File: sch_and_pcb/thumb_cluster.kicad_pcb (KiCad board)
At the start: 2 copper layers, 34 parts, among them J1 8PIN_CONN, J2 8PIN_CONN

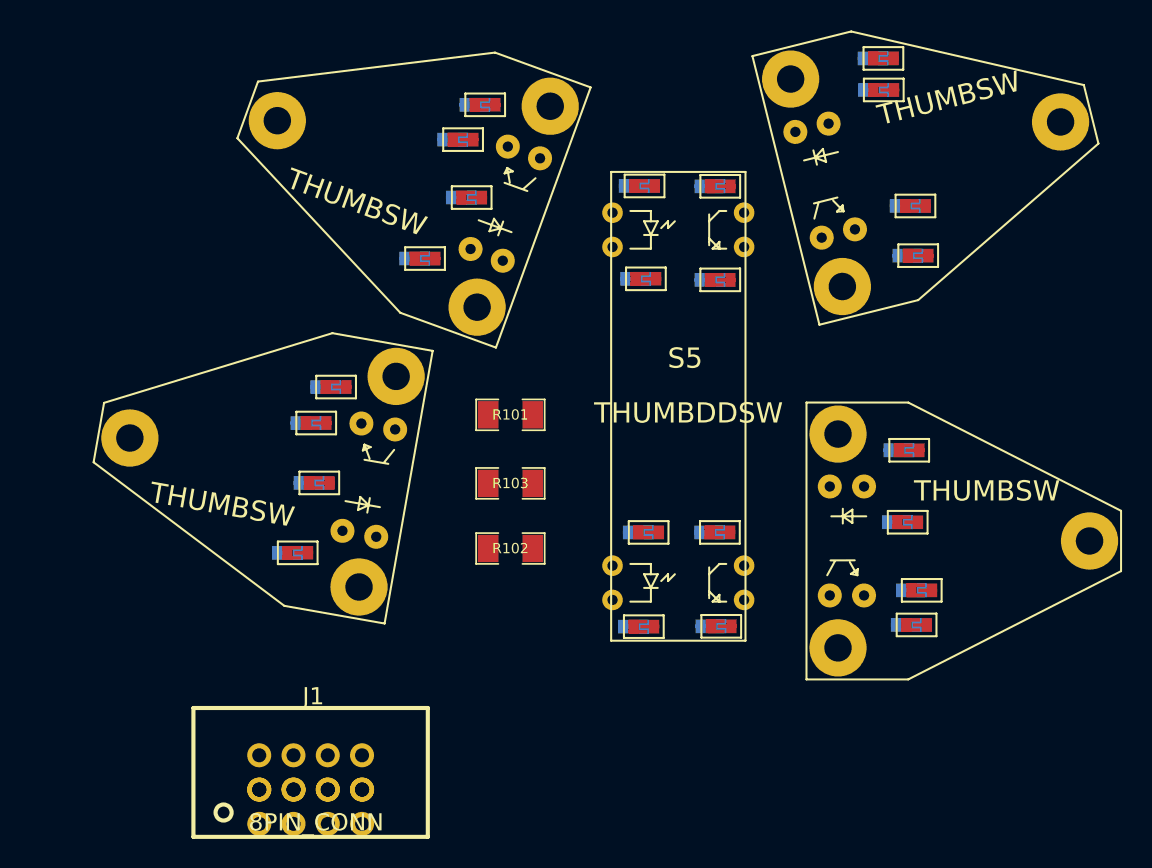
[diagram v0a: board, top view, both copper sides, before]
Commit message: PCB mostly routed. Shape not yet defined.
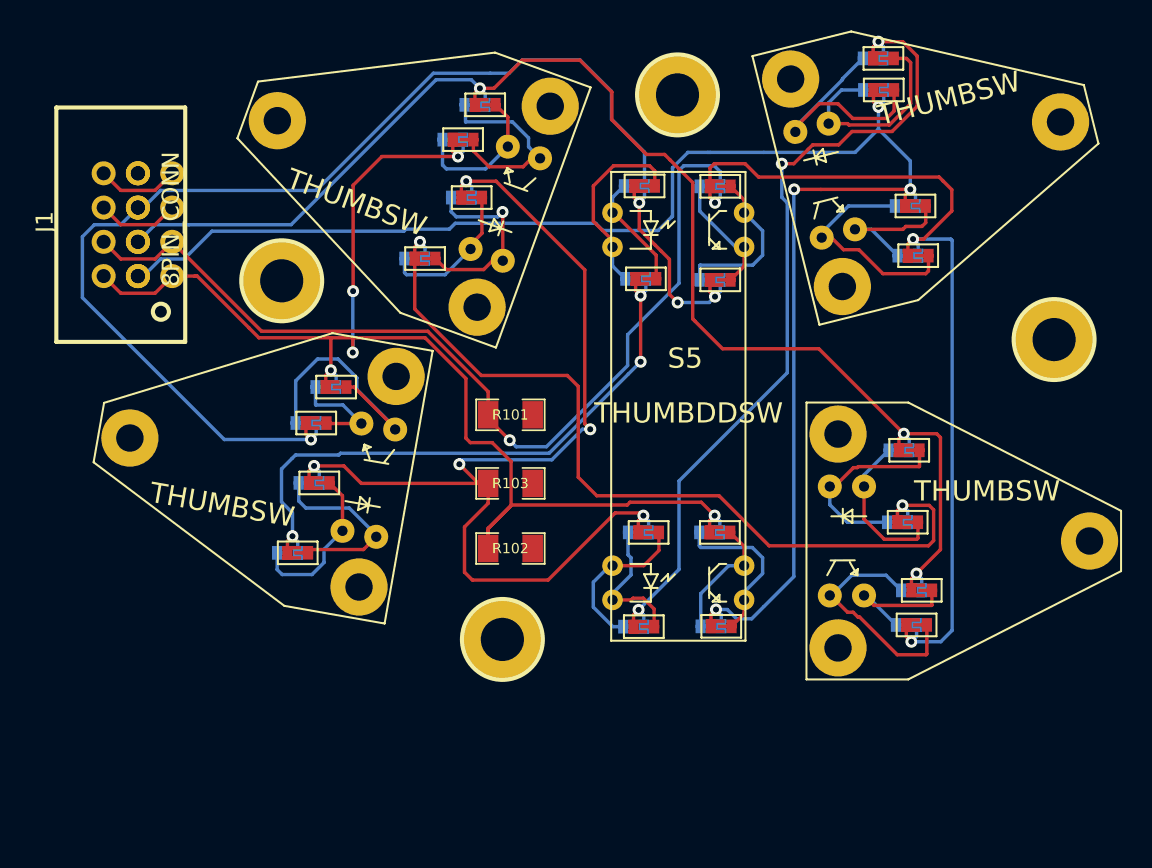
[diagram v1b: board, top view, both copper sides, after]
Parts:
- added M3_Mounting_Hole: VAL**, DodoHand:M3_Mounting_Hole, F.Cu at (-29.4, -9.30)
- added M3_Mounting_Hole: VAL**, DodoHand:M3_Mounting_Hole, F.Cu at (27.9, -4.95)
- added M3_Mounting_Hole: VAL**, DodoHand:M3_Mounting_Hole, F.Cu at (-13.0, 17.3)
- added M3_Mounting_Hole: VAL**, DodoHand:M3_Mounting_Hole, F.Cu at (-0.06, -23.1)
- moved J2 44.7 mm to (-38.8, -13.5), turned to 90 degrees
- moved J1 43.0 mm to (-41.3, -13.5), turned to 90 degrees
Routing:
- net /COL4: track 0.00 -> 139.4 mm, vias 0 -> 4
- net /ROW0: track 0.00 -> 122.1 mm, vias 0 -> 4
- net /ROW1: track 0.00 -> 103.5 mm, vias 0 -> 3
- net /ROW2: track 0.00 -> 99.3 mm, vias 0 -> 4
- net /COL5: track 0.00 -> 99.2 mm, vias 0 -> 5
- net Net-(R103-Pad1): track 0.00 -> 81.9 mm, vias 0 -> 5
- net Net-(SB5-Pad1): track 0.00 -> 63.9 mm, vias 0 -> 2
- net Net-(SB4-Pad1): track 0.00 -> 62.2 mm, vias 0 -> 3
- net Net-(SB6-Pad1): track 0.00 -> 45.7 mm, vias 0 -> 3
- net Net-(S4-Pad4): track 0.00 -> 19.5 mm
- net Net-(S1-Pad2): track 0.00 -> 18.8 mm
- net Net-(S3-Pad4): track 0.00 -> 18.2 mm
- net Net-(S1-Pad4): track 0.00 -> 17.5 mm
- net Net-(S1-Pad1): track 0.00 -> 16.7 mm
- net Net-(S2-Pad4): track 0.00 -> 15.5 mm
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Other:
- net class Default: clearance 0.254 -> 0.2286
- rule trace_clearance: 0.254 -> 0.2286
- rule trace_min: 0.254 -> 0.2286

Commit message: ground plane connected. silk cleanup still needed. soldermask slightly wrong on solder bridge. Needs corrected.
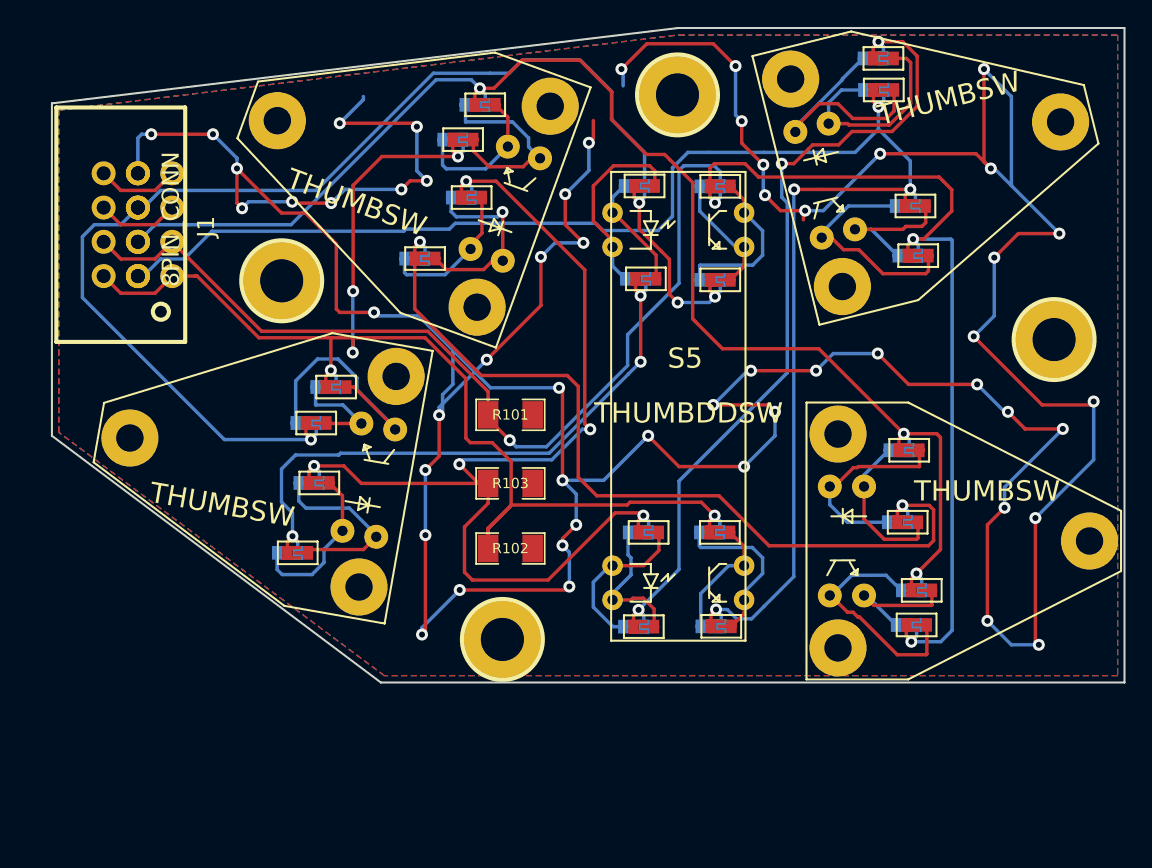
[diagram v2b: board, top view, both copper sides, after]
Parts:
- added G***: DHLOGO, DodoHand:DHLOGO, B.Cu at (-10.9, 2.13)
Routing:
- net GND: track 0.00 -> 340.6 mm, vias 0 -> 53
- added copper zone on B.Cu, net GND
- added copper zone on F.Cu, net GND
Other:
- board outline added: 79.5 x 48.5 mm
- net class Default: clearance 0.2286 -> 0.127
- rule trace_clearance: 0.2286 -> 0.127

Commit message: First pass of the Thumb Cluster PCB is complete.
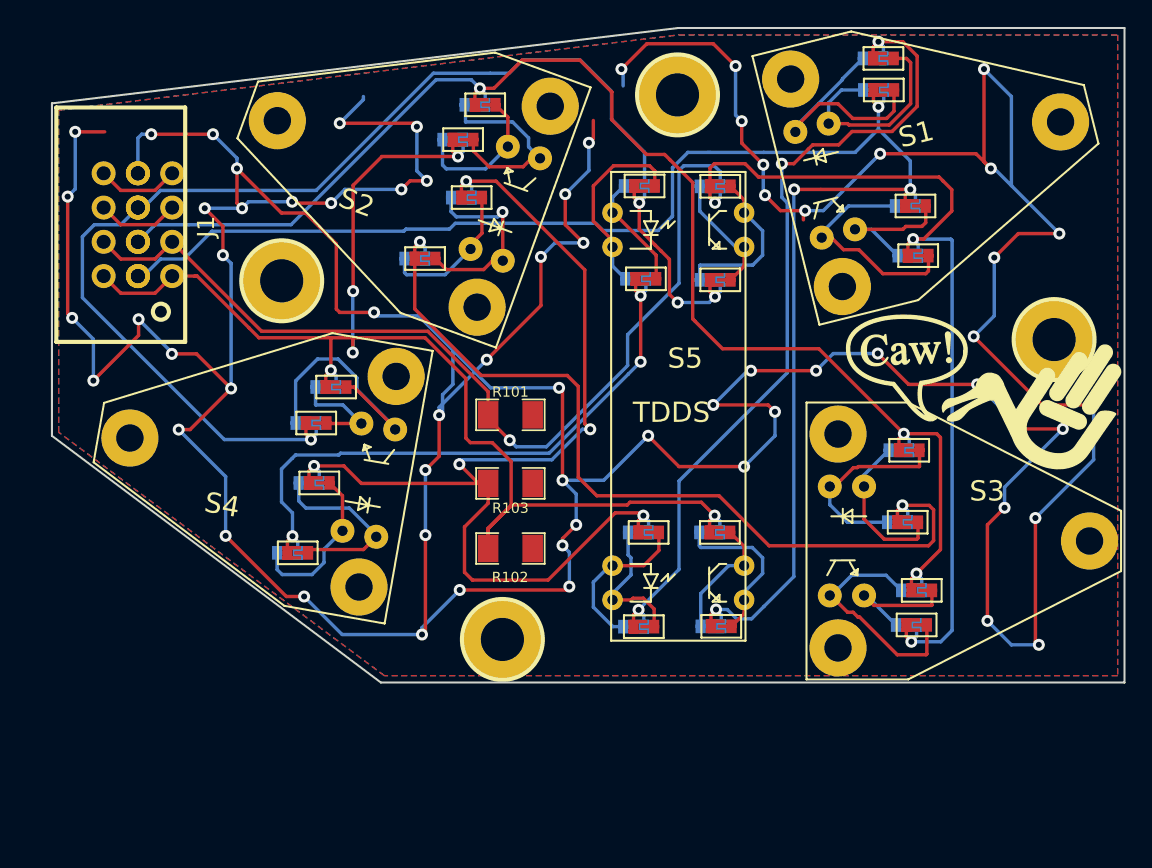
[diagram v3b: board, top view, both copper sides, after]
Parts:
- G***: moved to F.Cu
- S1: value THUMBSW -> S1
- S2: value THUMBSW -> S2
- S3: value THUMBSW -> S3
- S4: value THUMBSW -> S4
- S5: value THUMBDDSW -> TDDS
- moved G*** 33.7 mm to (22.6, -1.07), turned to 0 degrees
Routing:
- net GND: track 340.6 -> 426.2 mm, vias 53 -> 65
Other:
- board text added: "Solder bridges only on opposite side of opto parts."
- board text added: "Thanks to regack for the solder bridge science support"

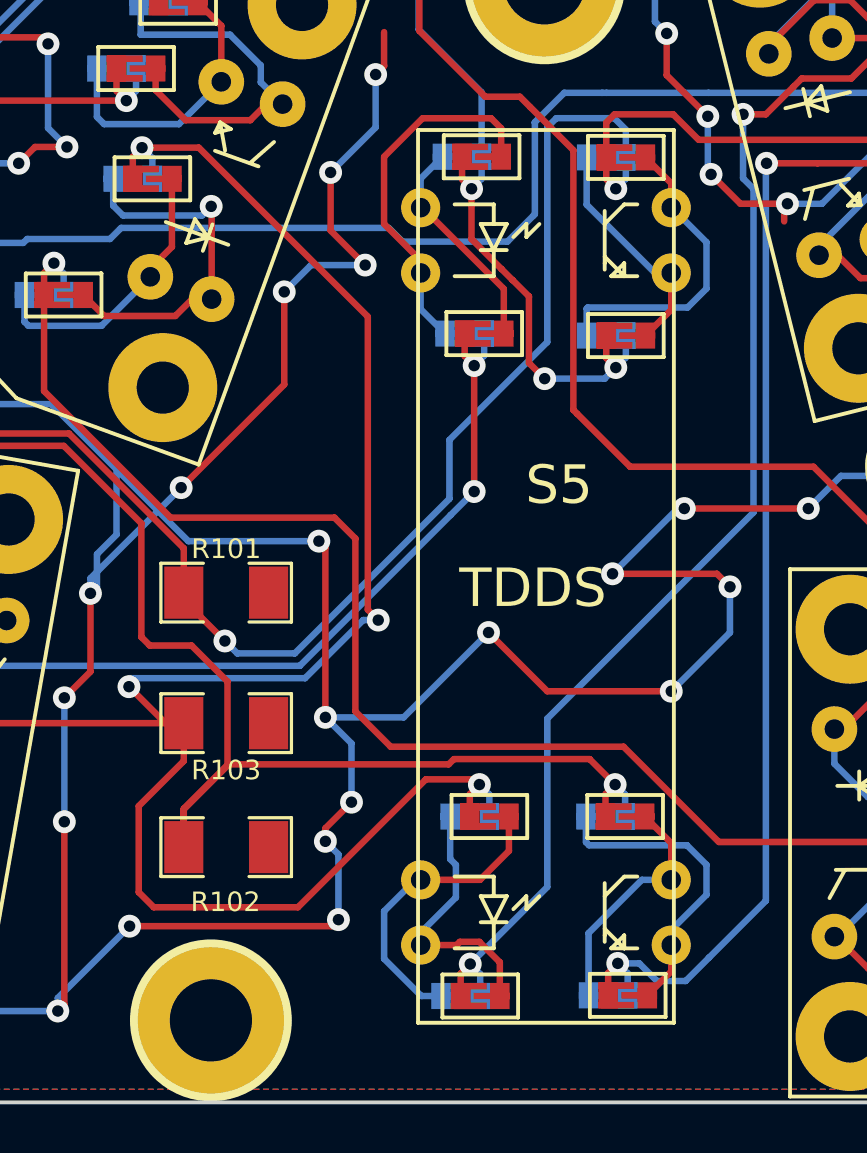
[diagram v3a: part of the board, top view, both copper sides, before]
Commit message: Corrected TDDS footprint, had to put it into new library in new .pretty directory format.
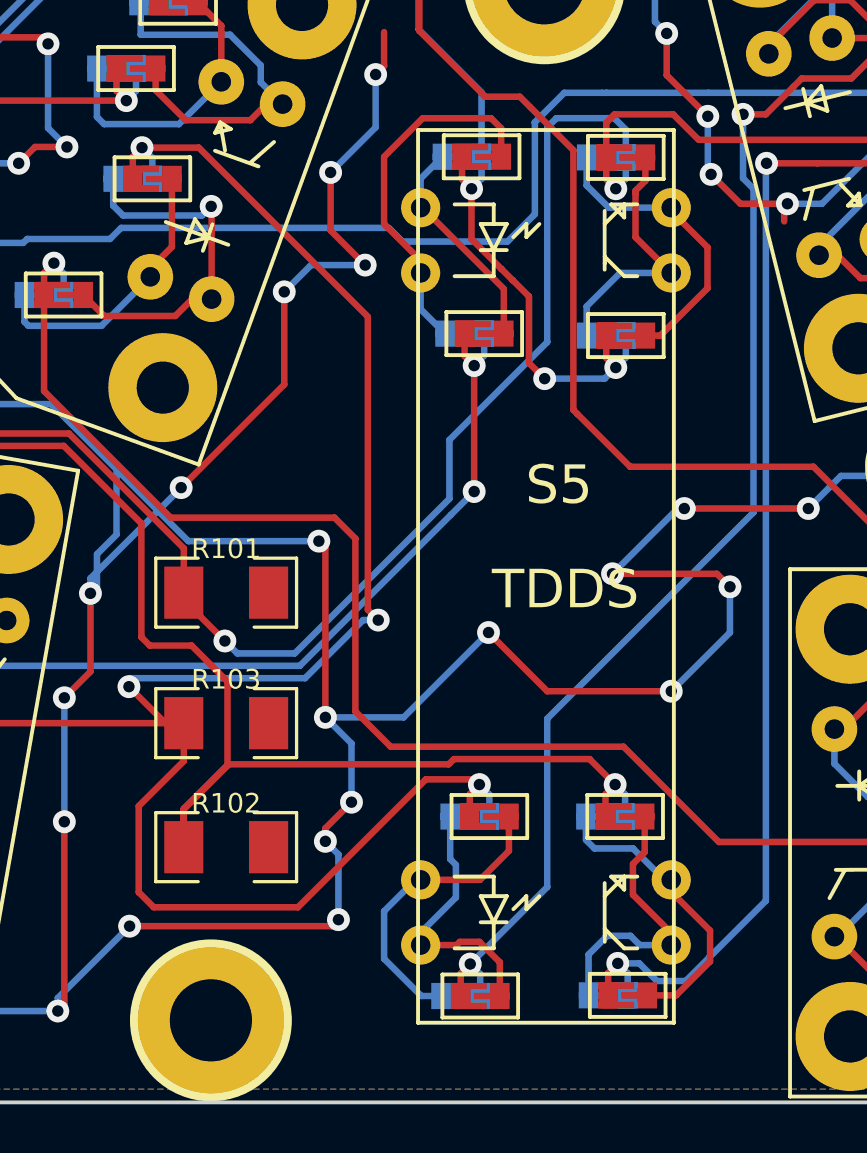
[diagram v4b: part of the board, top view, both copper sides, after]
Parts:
- R101, R102, R103: footprint divers:SM1206 -> DodoHand_New:SM1206
- S5: footprint DodoHand:TDDS -> DodoHand_New:TDDS
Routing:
- net Net-(S5-Pad7): track 9.72 -> 12.9 mm
- net Net-(S5-Pad6): track 10.0 -> 12.9 mm
- net Net-(S5-Pad8): track 12.8 -> 12.1 mm
